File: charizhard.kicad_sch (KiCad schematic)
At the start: 68 parts, among them J1 Conn_01x01_Pin, J11 Conn_01x01_Pin, J2 USB3_A Port USB, J3 Conn_01x01_Pin, J5 Molex5034801000 - Fingerprint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, U1 ESP32-WROOM-32, U2 LAN7800-I/Y9X USB-ETH Control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, U3 93AAxxAT-xOT, U4 LAN8720A-CP PHY, U5 AMS1117-3.3, Y1 ECS-250-18-33Q-DS, Y3 ECS-250-18-33Q-DS

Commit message: swap DI/DO on eeprom
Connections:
- net EEDI: now also U3.1 (DO); no longer U3.3 (DI)
- net EEDO: now also U3.3 (DI); no longer U3.1 (DO)
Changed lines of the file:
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@@
-		)
-	)
-	(label "EEDO"
-		(at 276.86 99.06 0)
-		(effects
-			(font
-				(size 1.27 1.27)
-			)
-			(justify left bottom)
 		)
 	)
@@
 		)
 	)
+	(label "EEDI"
+		(at 276.86 99.06 0)
+		(effects
+			(font
+				(size 1.27 1.27)
+			)
+			(justify left bottom)
+		)
+	)
 	(label "SENSOR_RST"
 		(at 320.04 154.94 180)
@@
 		)
 	)
-	(label "EEDI"
-		(at 276.86 96.52 0)
-		(effects
-			(font
-				(size 1.27 1.27)
-			)
-			(justify left bottom)
-		)
-	)
 	(label "PHY_RST"
 		(at 298.45 73.66 180)
@@
 		(effects
 			(font
+				(size 1.27 1.27)
+			)
+			(justify left bottom)
+		)
+	)
+	(label "EEDO"
+		(at 276.86 96.52 0)
+		(effects
+			(font

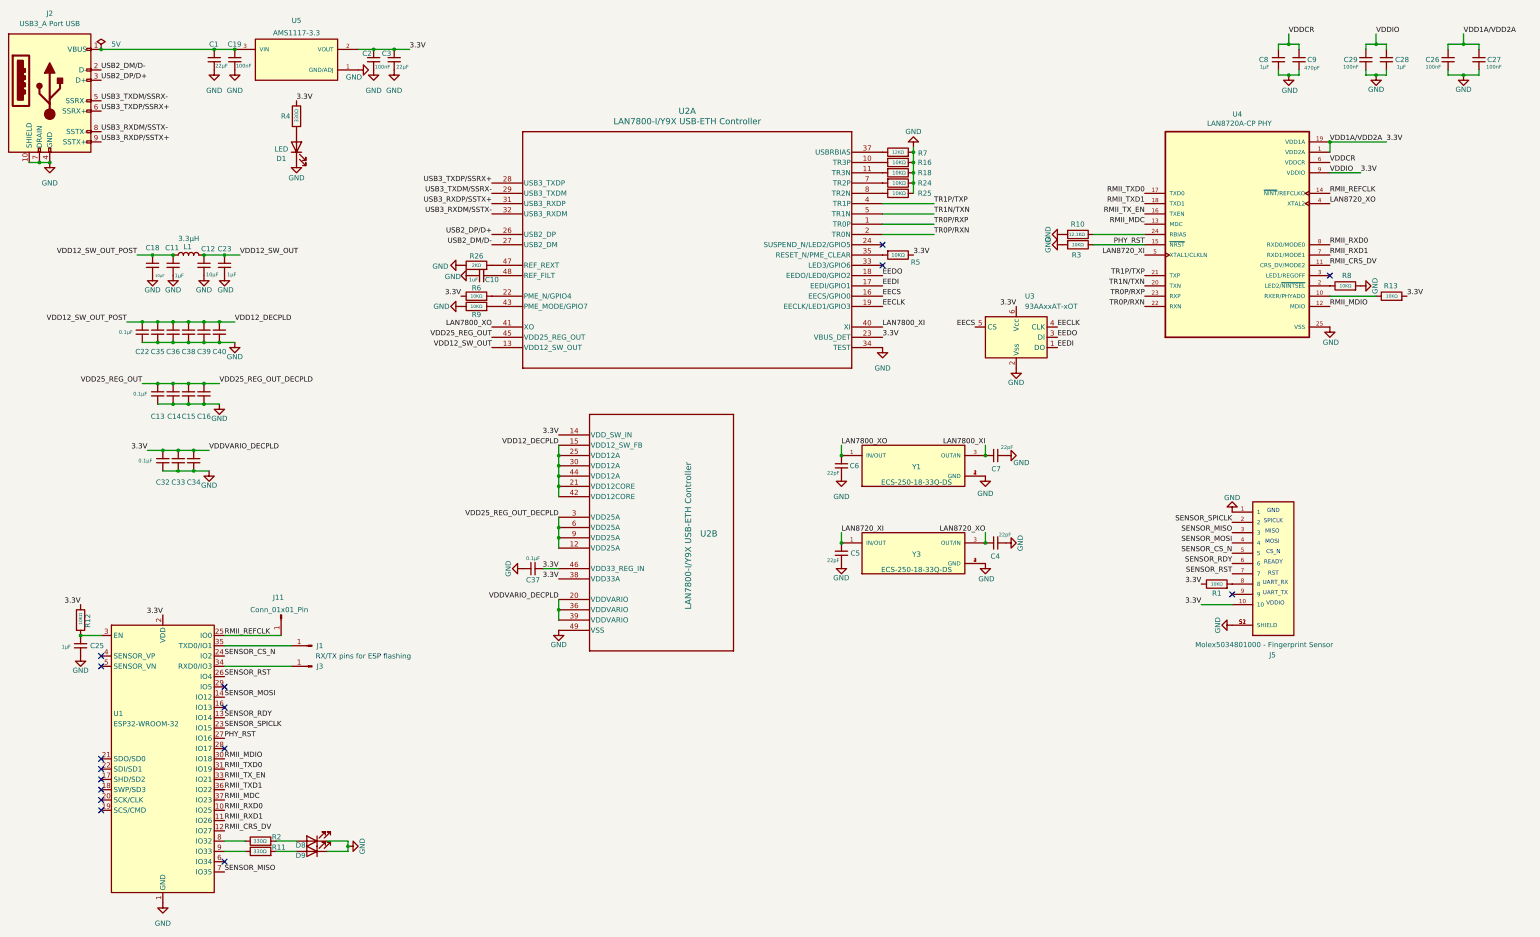
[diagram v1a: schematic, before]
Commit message: fix data lines noise+impedance
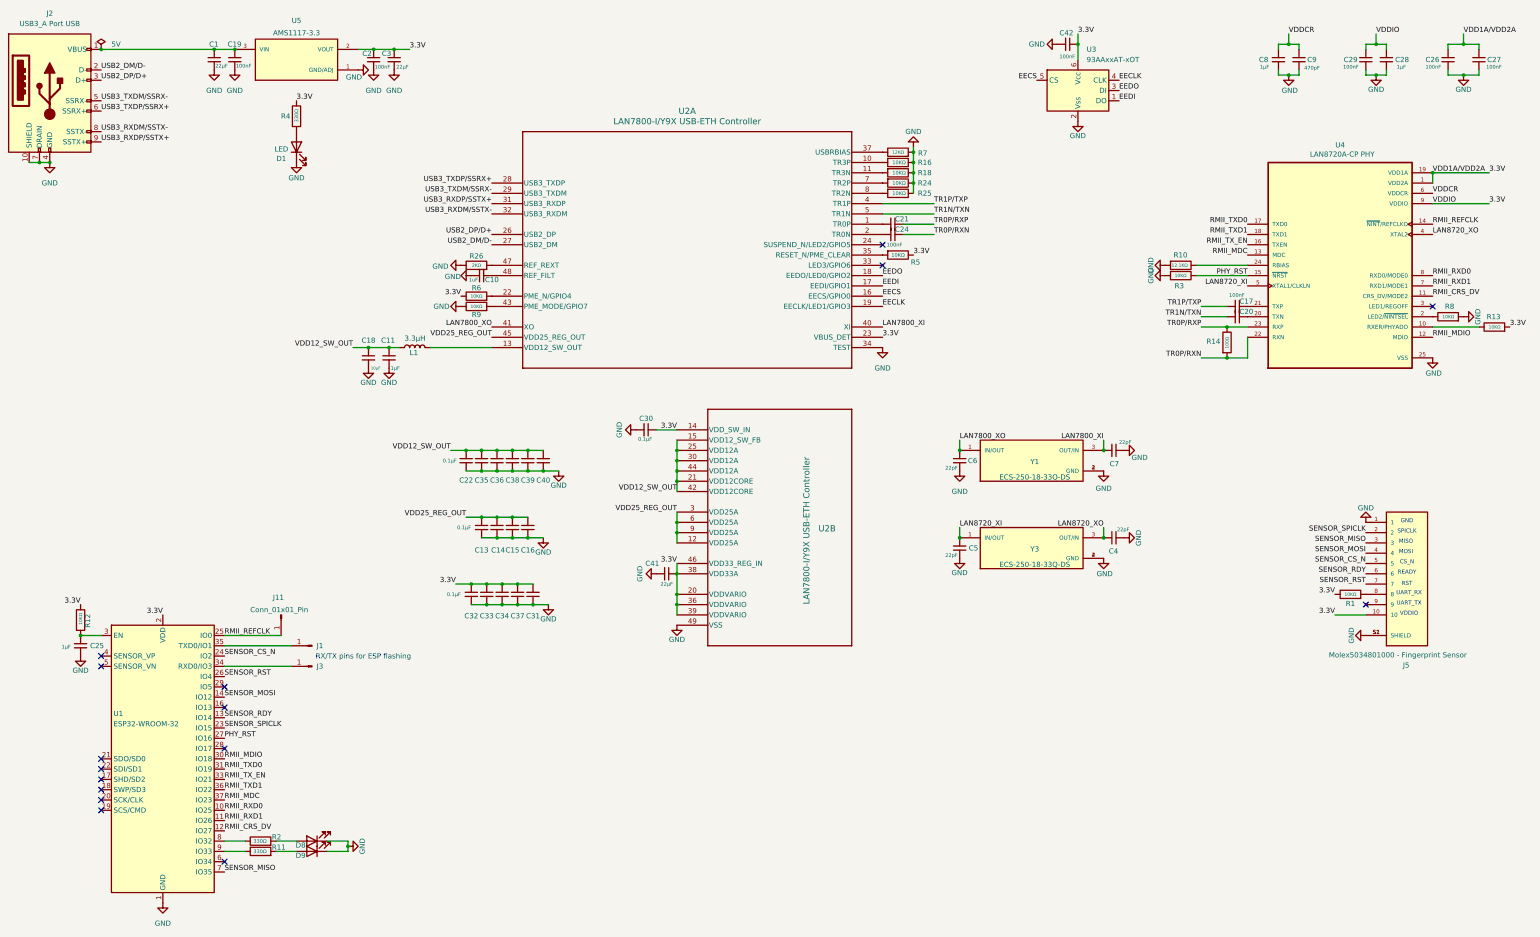
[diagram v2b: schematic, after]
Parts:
- removed C12: 10µF, Capacitor_SMD:C_0603_1608Metric, symbol Device:C_Small
- removed C23: 1µF, Capacitor_SMD:C_0603_1608Metric, symbol Device:C_Small
- added C17, C20, C21, C24, C42: 100nF, Capacitor_SMD:C_0603_1608Metric, symbol Device:C_Small
- added C30, C31: 0.1µF, Capacitor_SMD:C_0603_1608Metric, symbol Device:C_Small
- added C41: 22µF, Capacitor_SMD:C_0603_1608Metric, symbol Device:C_Small
- added R14: 100Ω, Resistor_SMD:R_0603_1608Metric, symbol Device:R
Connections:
- net VDD12_DECPLD is gone; now on net VDD12_SW_OUT: C11.1, C18.1, C22.1, C35.1, C36.1, C38.1, C39.2, C40.1, L1.1, U2.15 (VDD12_SW_FB), U2.21 (VDD12CORE), U2.25 (VDD12A), U2.30 (VDD12A), U2.42 (VDD12CORE), U2.44 (VDD12A)
- net 3.3V: now also C30.1, C31.2, C41.1, C42.1
- net GND: now also C30.2, C31.1, C41.2, C42.2
- net TR0P/RXN: now also C24.1, R14.2; no longer U2.2 (TR0N)
- net TR0P/RXP: now also C21.1, R14.1; no longer U2.1 (TR0P)
- net TR1N/TXN: now also C20.2; no longer U4.20 (TXN)
- net TR1P/TXP: now also C17.2; no longer U4.21 (TXP)
- net VDD12_SW_OUT: no longer L1.2, U2.13 (VDD12_SW_OUT)
- new net: C20.1, U4.20 (TXN)
- new net: C17.1, U4.21 (TXP)
- new net: C21.2, U2.1 (TR0P)
- new net: C24.2, U2.2 (TR0N)
- new net: L1.2, U2.13 (VDD12_SW_OUT)
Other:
- moved on the sheet: C11, C13, C14, C15, C16, C18, C22, C32, C33, C34, C35, C36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

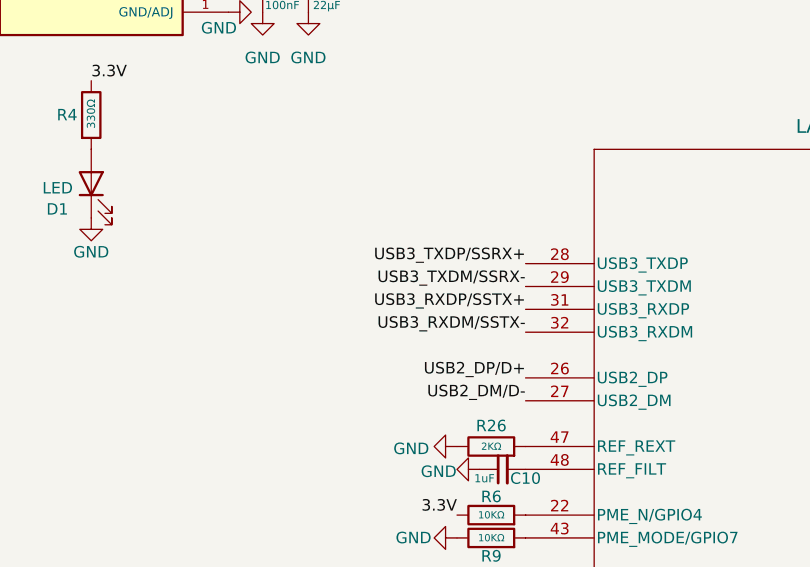
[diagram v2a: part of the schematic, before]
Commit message: add dc blocking caps on usb3 data line
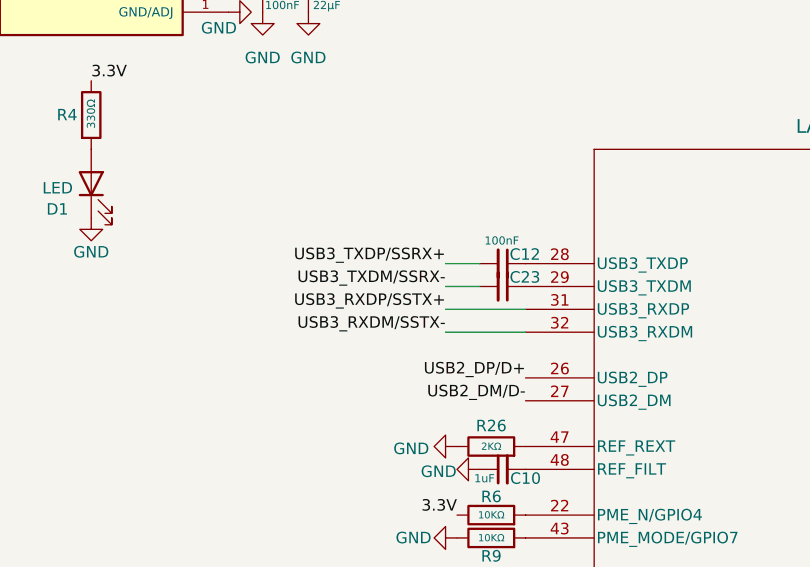
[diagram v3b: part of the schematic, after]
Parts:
- added C12, C23: 100nF, Capacitor_SMD:C_0603_1608Metric, symbol Device:C_Small
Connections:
- net USB3_TXDM/SSRX-: now also C23.2; no longer U2.29 (USB3_TXDM)
- net USB3_TXDP/SSRX+: now also C12.2; no longer U2.28 (USB3_TXDP)
- new net: C12.1, U2.28 (USB3_TXDP)
- new net: C23.1, U2.29 (USB3_TXDM)
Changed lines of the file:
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@@
 	(wire
 		(pts
+			(xy 128.27 63.5) (xy 137.16 63.5)
+		)
+		(stroke
+			(width 0)
+			(type default)
+		)
+	)
+	(wire
+		(pts
 			(xy 281.94 24.13) (xy 281.94 27.94)
 		)
@@
 	(wire
 		(pts
+			(xy 128.27 60.96) (xy 132.08 60.96)
+		)
+		(stroke
+			(width 0)
+			(type default)
+		)
+	)
+	(wire
+		(pts
 			(xy 288.29 143.51) (xy 288.29 146.05)
 		)
@@
 	(wire
 		(pts
+			(xy 128.27 58.42) (xy 132.08 58.42)
+		)
+		(stroke
+			(width 0)
+			(type default)
+		)
+	)
+	(wire
+		(pts
 			(xy 143.51 162.56) (xy 139.7 162.56)
 		)
@@
 	(wire
 		(pts
+			(xy 128.27 66.04) (xy 137.16 66.04)
+		)
+		(stroke
+			(width 0)
+			(type default)
+		)
+	)
+	(wire
+		(pts
 			(xy 312.42 91.44) (xy 318.77 91.44)
 		)
@@
 	)
 	(label "USB3_TXDM{slash}SSRX-"
-		(at 137.16 60.96 180)
+		(at 128.27 60.96 180)
 		(effects
 			(font
@@
 	)
 	(label "USB3_RXDP{slash}SSTX+"
-		(at 137.16 63.5 180)
+		(at 128.27 63.5 180)
 		(effects
 			(font
@@
 	)
 	(label "USB3_TXDP{slash}SSRX+"
-		(at 137.16 58.42 180)
+		(at 128.27 58.42 180)
 		(effects
 			(font
@@
 	)
 	(label "USB3_RXDM{slash}SSTX-"
-		(at 137.16 66.04 180)
+		(at 128.27 66.04 180)
 		(effects
 			(font
@@
 	)
 	(symbol
+		(lib_id "Device:C_Small")
+		(at 134.62 58.42 270)
+		(unit 1)
+		(exclude_from_sim no)
+		(in_bom yes)
+		(on_board yes)
+		(dnp no)
+		(property "Reference" "C12"
+			(at 135.382 57.404 90)
+			(effects
+				(font
+					(size 1.27 1.27)
+				)
+				(justify left)
+			)
+		)
+		(property "Value" "100nF"
+			(at 132.588 55.88 90)
+			(effects
+				(font
+					(size 0.9 0.9)
+				)
+				(justify left)
+			)
+		)
+		(property "Footprint" "Capacitor_SMD:C_0603_1608Metric"
+			(at 134.62 58.42 0)
+			(effects
+				(font
+					(size 1.27 1.27)
+				)
+				(hide yes)
+			)
+		)
+		(property "Datasheet" "~"
+			(at 134.62 58.42 0)
+			(effects
+				(font
+					(size 1.27 1.27)
+				)
+				(hide yes)
+			)
+		)
+		(property "Description" "Unpolarized capacitor, small symbol"
+			(at 134.62 58.42 0)
+			(effects
+				(font
+					(size 1.27 1.27)
+				)
+				(hide yes)
+			)
+		)
+		(pin "2"
+		)
+		(pin "1"
+		)
+		(instances
+			(project "charizhard"
+				(path "/5faa4c25-1746-428d-9bc9-7befcb644a99"
+					(reference "C12")
+					(unit 1)
+				)
+			)
+		)
+	)
+	(symbol
 		(lib_id "ECS-250-18-33Q-DS:ECS-250-18-33Q-DS")
 		(at 270.51 148.59 0)
@@
 					(unit 1)
 				)
+			)
+		)
+	)
+	(symbol
+		(lib_id "Device:C_Small")
+		(at 134.62 60.96 270)
+		(unit 1)
+		(exclude_from_sim no)
+		(in_bom yes)
+		(on_board yes)
+		(dnp no)
+		(property "Reference" "C23"
+			(at 135.382 59.944 90)
+			(effects
+				(font
+					(size 1.27 1.27)
+				)
+				(justify left)
+			)
+		)
+		(property "Value" "100nF"
+			(at 132.842 61.214 0)
+			(effects
+				(font
+					(size 0.9 0.9)
+				)
+				(justify left)
+				(hide yes)
+			)
+		)
+		(property "Footprint" "Capacitor_SMD:C_0603_1608Metric"
+			(at 134.62 60.96 0)
+			(effects
+				(font
+					(size 1.27 1.27)
+				)
+				(hide yes)
+			)
+		)
+		(property "Datasheet" "~"
+			(at 134.62 60.96 0)
+			(effects
+				(font
+					(size 1.27 1.27)
+				)
+				(hide yes)
+			)
+		)
+		(property "Description" "Unpolarized capacitor, small symbol"
+			(at 134.62 60.96 0)
+			(effects
+				(font
+					(size 1.27 1.27)
+				)
+				(hide yes)
+			)
+		)
+		(pin "2"
+		)
+		(pin "1"
+		)
+		(instances
+			(project "charizhard"
+				(path "/5faa4c25-1746-428d-9bc9-7befcb644a99"
+					(reference "C23")
+					(unit 1)
+				)

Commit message: remove useless res
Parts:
- removed R14: 100Ω, Resistor_SMD:R_0603_1608Metric, symbol Device:R
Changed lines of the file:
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@@
 	)
 	(junction
-		(at 318.77 101.6)
-		(diameter 0)
-		(color 0 0 0 0)
-	)
-	(junction
 		(at 281.94 24.13)
 		(diameter 0)
@@
 	)
 	(junction
-		(at 318.77 93.98)
-		(diameter 0)
-		(color 0 0 0 0)
-	)
-	(junction
 		(at 182.88 142.24)
 		(diameter 0)
@@
 	(wire
 		(pts
-			(xy 318.77 93.98) (xy 323.85 93.98)
+			(xy 312.42 93.98) (xy 323.85 93.98)
 		)
 		(stroke
@@
 	(wire
 		(pts
-			(xy 312.42 101.6) (xy 318.77 101.6)
-		)
-		(stroke
-			(width 0)
-			(type default)
-		)
-	)
-	(wire
-		(pts
 			(xy 134.62 140.97) (xy 138.43 140.97)
 		)
@@
 	(wire
 		(pts
-			(xy 323.85 101.6) (xy 323.85 96.52)
-		)
-		(stroke
-			(width 0)
-			(type default)
-		)
-	)
-	(wire
-		(pts
 			(xy 182.88 154.94) (xy 182.88 160.02)
 		)
@@
 	(wire
 		(pts
-			(xy 312.42 93.98) (xy 318.77 93.98)
-		)
-		(stroke
-			(width 0)
-			(type default)
-		)
-	)
-	(wire
-		(pts
 			(xy 381 93.98) (xy 369.57 93.98)
 		)
@@
 	(wire
 		(pts
-			(xy 318.77 101.6) (xy 323.85 101.6)
+			(xy 312.42 96.52) (xy 323.85 96.52)
 		)
 		(stroke
@@
 	)
 	(label "TR0P{slash}RXN"
-		(at 312.42 101.6 180)
+		(at 312.42 96.52 180)
 		(effects
 			(font
@@
 					(unit 1)
 				)
-			)
-		)
-	)
-	(symbol
-		(lib_id "Device:R")
-		(at 318.77 97.79 0)
-		(unit 1)
-		(exclude_from_sim no)
-		(in_bom yes)
-		(on_board yes)
-		(dnp no)
-		(property "Reference" "R14"
-			(at 313.69 97.536 0)
-			(effects
-				(font
-					(size 1.27 1.27)
-				)
-				(justify left)
-			)
-		)
-		(property "Value" "100Ω"
-			(at 318.77 99.314 90)
-			(effects
-				(font
-					(size 0.8 0.8)
-				)
-				(justify left)
-			)
-		)
-		(property "Footprint" "Resistor_SMD:R_0603_1608Metric"
-			(at 316.992 97.79 90)
-			(effects
-				(font
-					(size 1.27 1.27)
-				)
-				(hide yes)
-			)
-		)
-		(property "Datasheet" "~"
-			(at 318.77 97.79 0)
-			(effects
-				(font
-					(size 1.27 1.27)
-				)
-				(hide yes)
-			)
-		)
-		(property "Description" "Resistor"
-			(at 318.77 97.79 0)
-			(effects
-				(font
-					(size 1.27 1.27)
-				)
-				(hide yes)
-			)
-		)
-		(pin "2"
-		)
-		(pin "1"
-		)
-		(instances
-			(project "charizhard"
-				(path "/5faa4c25-1746-428d-9bc9-7befcb644a99"
-					(reference "R14")
-					(unit 1)
-				)

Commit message: fixes?
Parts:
- J5: footprint MOLEX5034801000:MOLEX_5034801000 -> 5034801000:MOLEX_5034801000; Description_1 503480 Series 0.5mm Pitch 10 Way Right Angle SMT Male FPC Connector, Solder | Molex Incorporated 503480-1000 -> 503480 Series 0.5mm Pitch 10 Way Right Angle SMT Male FPC Connector, Solder | Molex Incorporated 503480-1000
- U2: footprint LAN7800:48SQFN-5304-7X7B_MCH -> 48SQFN-5304-7X7B_MCH
- U4: footprint LAN8720A:QFN50P400X400X100-25N -> LAN8720A-CP:QFN50P400X400X100-25N; Description_1 2/2 Transceiver Full RMII 24-QFN-EP (4x4) -> 2/2 Transceiver Full RMII 24-QFN-EP (4x4)
- Y1, Y3: footprint Crystal SMB 25MHz 3225:XTAL_ECS-250-18-33Q-DS -> ECS-250-18-33Q-DS:XTAL_ECS-250-18-33Q-DS; Description_1 25 MHz ±30ppm Crystal 18pF 40 Ohms 4-SMD, No Lead -> 25 MHz ±30ppm Crystal 18pF 40 Ohms 4-SMD, No Lead
